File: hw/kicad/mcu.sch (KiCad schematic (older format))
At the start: 23 parts

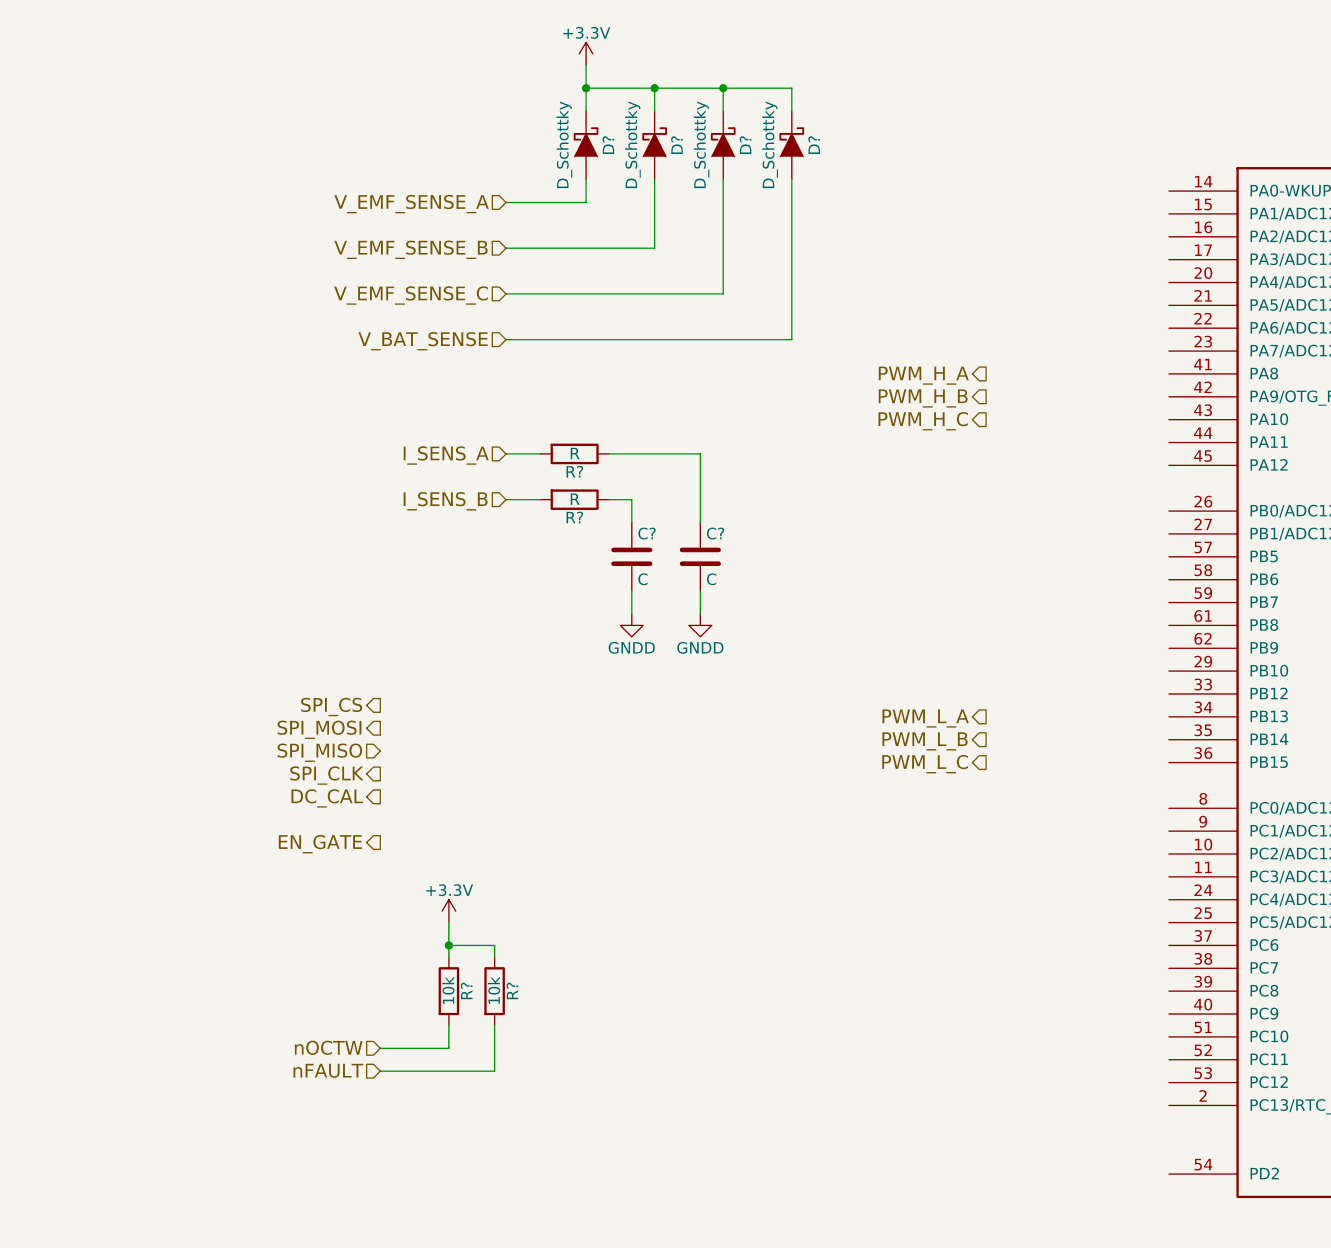
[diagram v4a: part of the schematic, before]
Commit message: Connect mcu to drv8301
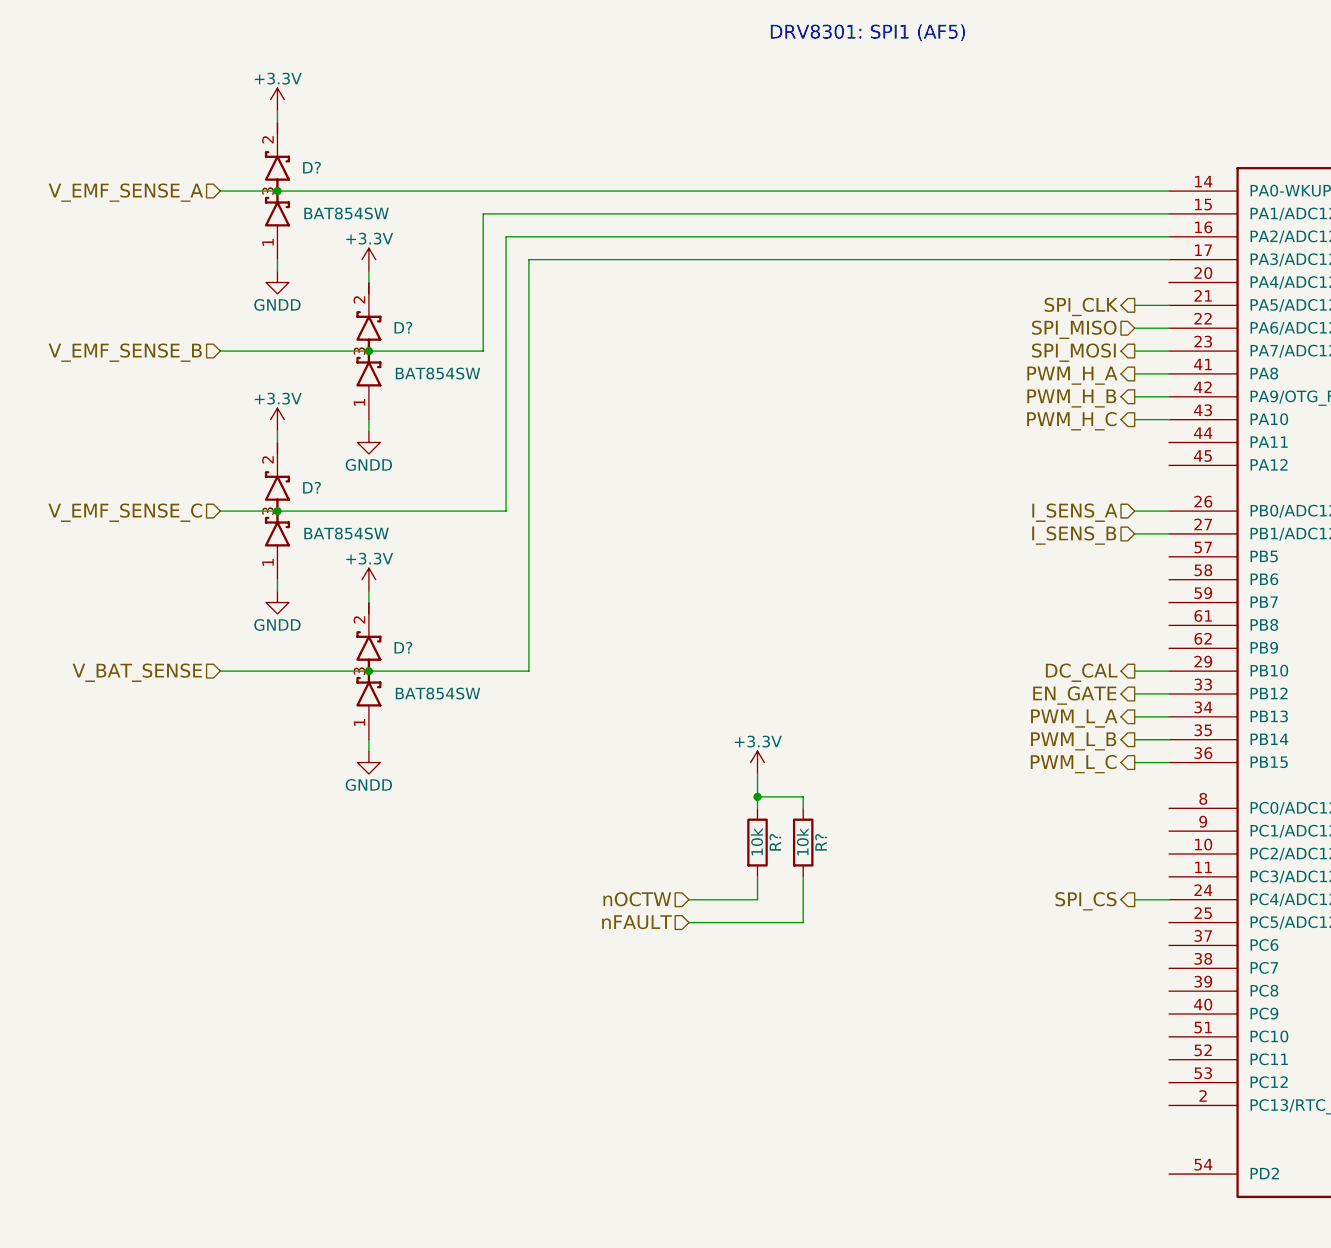
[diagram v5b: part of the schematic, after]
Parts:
- removed C? (x2): C, symbol C
- removed D? (x4): D_Schottky, symbol D_Schottky
- removed R? (x2): R, symbol R
- added D? (x4): BAT854SW, TO_SOT_Packages_SMD:SOT-323, symbol D_Schottky_x2_Serial_AKC
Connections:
- net +3V3: now also D?.2 (K), D?.2 (K), D?.2 (K), D?.2 (K)
- net DC_CAL: now also U?.29 (PB10)
- net EN_GATE: now also U?.33 (PB12)
- net GNDD: now also D?.1 (A), D?.1 (A), D?.1 (A), D?.1 (A)
- net I_SENS_A: now also U?.26 (PB0/ADC12_IN8)
- net I_SENS_B: now also U?.27 (PB1/ADC12_IN9)
- net PWM_H_A: now also U?.41 (PA8)
- net PWM_H_B: now also U?.42 (PA9/OTG_FS_VBUS)
- net PWM_H_C: now also U?.43 (PA10)
- net PWM_L_A: now also U?.34 (PB13)
- net PWM_L_B: now also U?.35 (PB14)
- net PWM_L_C: now also U?.36 (PB15)
- net SPI_CLK: now also U?.21 (PA5/ADC12_IN5/DAC_OUT2)
- net SPI_CS: now also U?.24 (PC4/ADC12_IN14)
- net SPI_MISO: now also U?.22 (PA6/ADC12_IN6)
- net SPI_MOSI: now also U?.23 (PA7/ADC12_IN7)
- net V_BAT_SENSE: now also U?.17 (PA3/ADC123_IN3), D?.3 (common)
- net V_EMF_SENSE_A: now also U?.14 (PA0-WKUP/ADC123_IN0), D?.3 (common)
- net V_EMF_SENSE_B: now also U?.15 (PA1/ADC123_IN1), D?.3 (common)
- net V_EMF_SENSE_C: now also U?.16 (PA2/ADC123_IN2), D?.3 (common)
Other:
- note added: "DRV8301: SPI1 (AF5)"
- moved on the sheet: R?

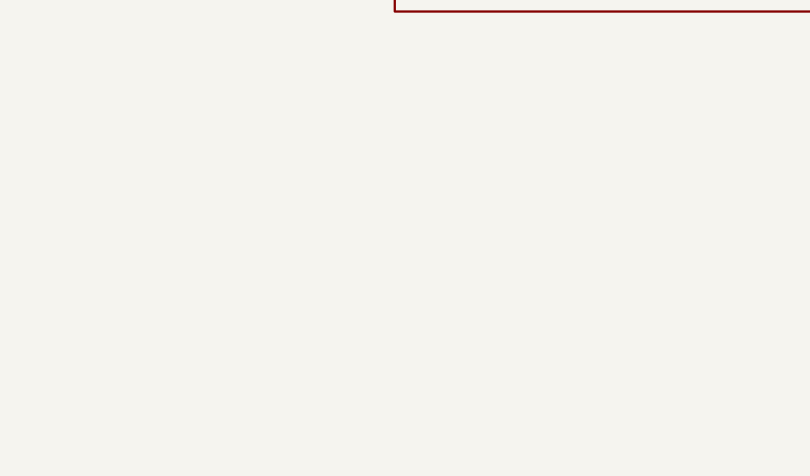
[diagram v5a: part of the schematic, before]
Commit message: Added LDO for mcu
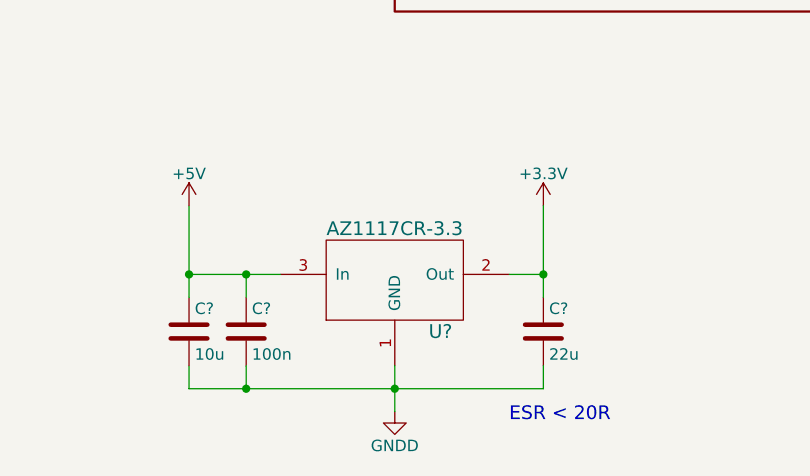
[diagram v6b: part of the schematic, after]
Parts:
- added C?: 100n, symbol C
- added C?: 22u, symbol C
- added C?: 10u, symbol C
- added U?: AZ1117CR-3.3, TO_SOT_Packages_SMD:SOT89-3_Housing, symbol AZ1117CR-3.3
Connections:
- net +3V3: now also C?.1, U?.2 (Out)
- net GNDD: now also C?.2, C?.2, C?.2, U?.1 (GND)
- new net +5V: C?.1, C?.1, U?.3 (In)
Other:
- note added: "ESR < 20R"
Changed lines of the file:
@@
 LIBS:wslp2726
 LIBS:test
+LIBS:az1117c
 LIBS:MotCtrl-cache
 EELAYER 25 0
@@
 Wire Wire Line
 	5350 3400 5500 3400
+$Comp
+L +5V #PWR?
+U 1 1 5823AFF4
+P 4900 6550
+F 0 "#PWR?" H 4900 6400 50  0001 C CNN
+F 1 "+5V" H 4900 6690 50  0000 C CNN
+F 2 "" H 4900 6550 60  0000 C CNN
+F 3 "" H 4900 6550 60  0000 C CNN
+	1    4900 6550
+	1    0    0    -1
+$EndComp
+$Comp
+L +3.3V #PWR?
+U 1 1 5823B078
+P 6450 6550
+F 0 "#PWR?" H 6450 6400 50  0001 C CNN
+F 1 "+3.3V" H 6450 6690 50  0000 C CNN
+F 2 "" H 6450 6550 60  0000 C CNN
+F 3 "" H 6450 6550 60  0000 C CNN
+	1    6450 6550
+	1    0    0    -1
+$EndComp
+$Comp
+L GNDD #PWR?
+U 1 1 5823B0BC
+P 5800 7450
+F 0 "#PWR?" H 5800 7200 50  0001 C CNN
+F 1 "GNDD" H 5800 7300 50  0000 C CNN
+F 2 "" H 5800 7450 60  0000 C CNN
+F 3 "" H 5800 7450 60  0000 C CNN
+	1    5800 7450
+	1    0    0    -1
+$EndComp
+$Comp
+L AZ1117CR-3.3 U?
+U 1 1 5823B559
+P 5800 6850
+F 0 "U?" H 6000 6600 60  0000 C CNN
+F 1 "AZ1117CR-3.3" H 5800 7050 60  0000 C CNN
+F 2 "TO_SOT_Packages_SMD:SOT89-3_Housing" H 5800 6850 60  0001 C CNN
+F 3 "" H 5800 6850 60  0001 C CNN
+	1    5800 6850
+	1    0    0    -1
+$EndComp
+$Comp
+L C C?
+U 1 1 5823B6C8
+P 5150 7100
+F 0 "C?" H 5175 7200 50  0000 L CNN
+F 1 "100n" H 5175 7000 50  0000 L CNN
+F 2 "" H 5188 6950 30  0000 C CNN
+F 3 "" H 5150 7100 60  0000 C CNN
+	1    5150 7100
+	1    0    0    -1
+$EndComp
+$Comp
+L C C?
+U 1 1 5823B818
+P 6450 7100
+F 0 "C?" H 6475 7200 50  0000 L CNN
+F 1 "22u" H 6475 7000 50  0000 L CNN
+F 2 "" H 6488 6950 30  0000 C CNN
+F 3 "" H 6450 7100 60  0000 C CNN
+	1    6450 7100
+	1    0    0    -1
+$EndComp
+Wire Wire Line
+	5150 6950 5150 6850
+Wire Wire Line
+	4900 6850 5300 6850
+Wire Wire Line
+	6300 6850 6450 6850
+Wire Wire Line
+	6450 6550 6450 6950
+Wire Wire Line
+	5800 7450 5800 7250
+Wire Wire Line
+	4900 7350 6450 7350
+Wire Wire Line
+	6450 7350 6450 7250
+Connection ~ 5800 7350
+Wire Wire Line
+	5150 7350 5150 7250
+$Comp
+L C C?
+U 1 1 5823BE21
+P 4900 7100
+F 0 "C?" H 4925 7200 50  0000 L CNN
+F 1 "10u" H 4925 7000 50  0000 L CNN
+F 2 "" H 4938 6950 30  0000 C CNN
+F 3 "" H 4900 7100 60  0000 C CNN
+	1    4900 7100
+	1    0    0    -1
+$EndComp
+Wire Wire Line
+	4900 7350 4900 7250
+Connection ~ 5150 7350
+Wire Wire Line
+	4900 6550 4900 6950
+Connection ~ 5150 6850
+Connection ~ 4900 6850
+Connection ~ 6450 6850
+Text Notes 6300 7500 0    60   ~ 0
+ESR < 20R
 $EndSCHEMATC

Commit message: work
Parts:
- added C? (x4): 4n7, symbol C
- added P?: CONN_01X06, symbol CONN_01X06
- added R? (x3): 2k2, symbol R
- added R? (x4): 10k, symbol R
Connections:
- net +3V3: now also R?.1, R?.1, R?.1, R?.1
- net +5V: now also P?.1 (P1)
- net GNDD: now also C?.2, C?.2, C?.2, C?.2, P?.6 (P6)
- new net: P?.3 (P3), R?.2, R?.2
- new net: P?.4 (P4), R?.2, R?.2
- new net: P?.5 (P5), R?.2, R?.2
- new net HALL_1: C?.1, R?.1
- new net HALL_2: C?.1, R?.1
- new net HALL_3: C?.1, R?.1
- new net MOT_TEMP: C?.1, P?.2 (P2), R?.2
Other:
- moved on the sheet: R?

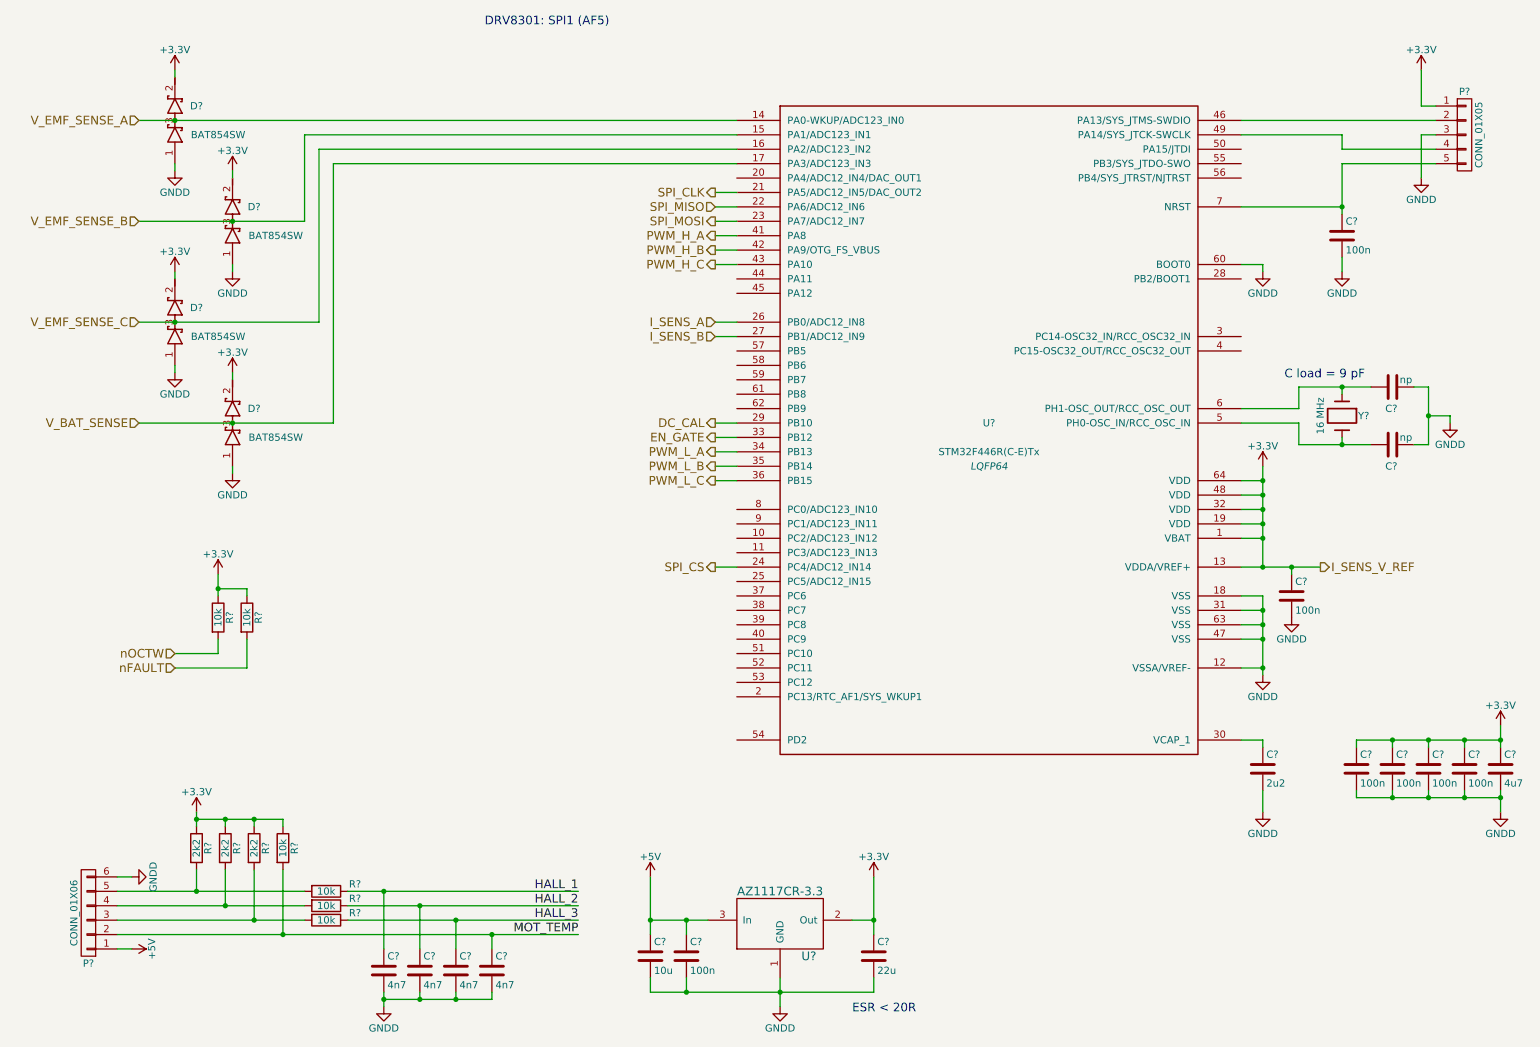
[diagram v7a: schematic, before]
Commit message: Big changes in power: new mosfets, drivers and current sensing
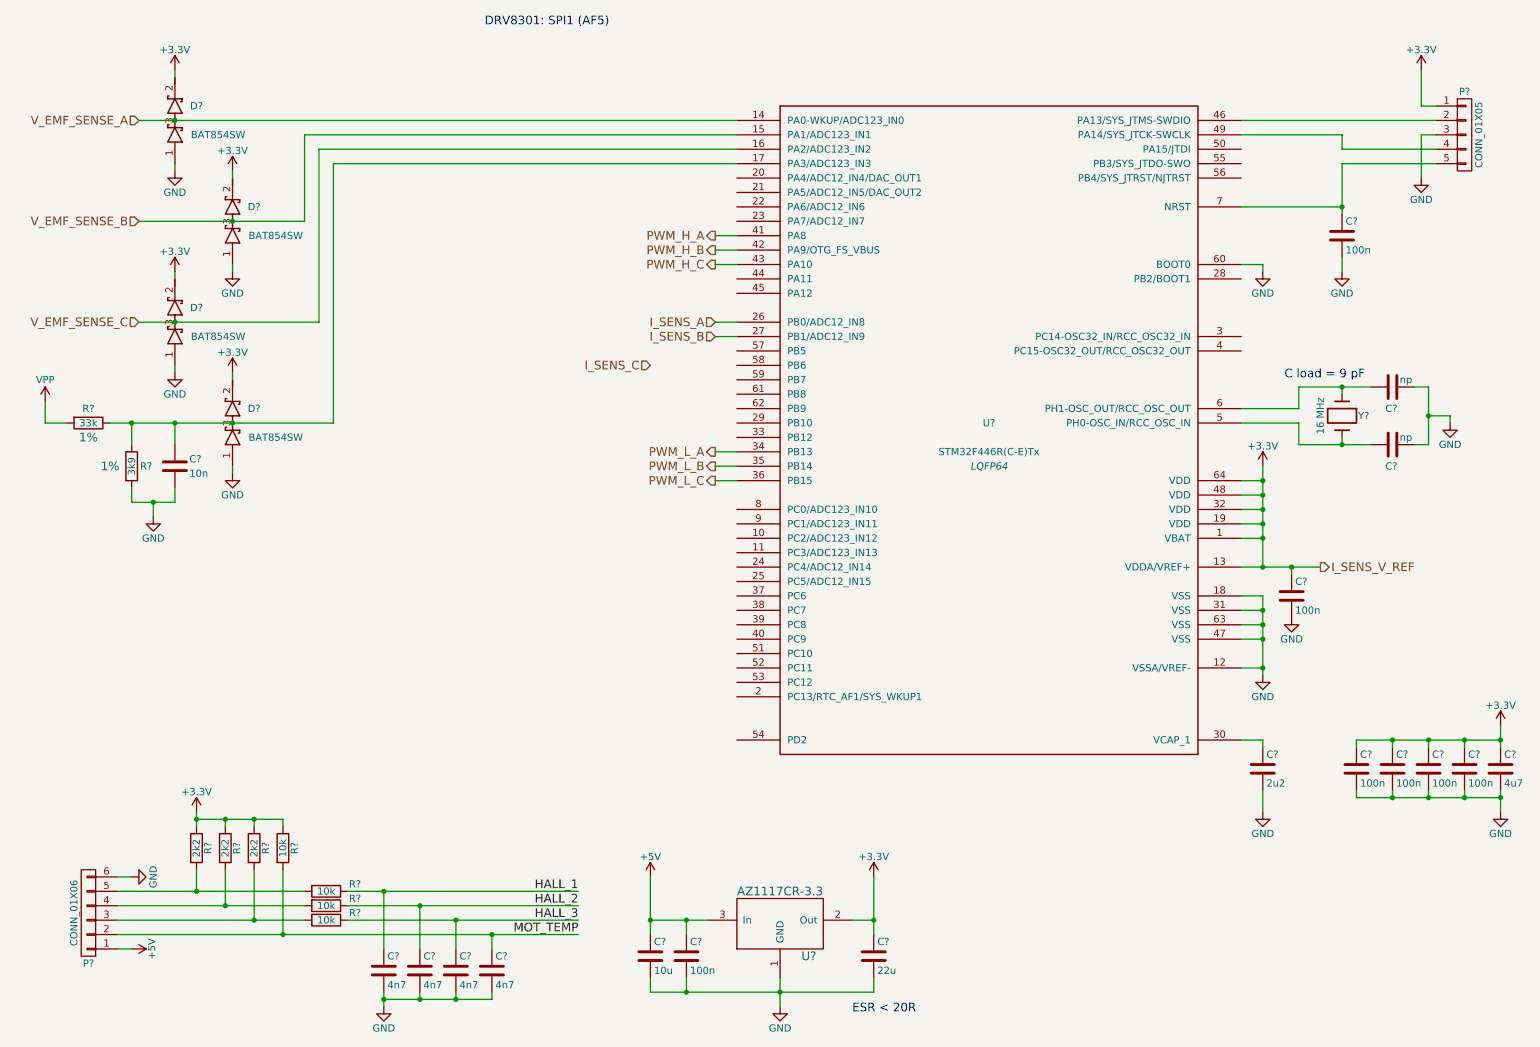
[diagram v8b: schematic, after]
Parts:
- removed R? (x2): 10k, symbol R
- added C?: 10n, symbol C
- added R?: 33k, symbol R
- added R?: 3k9, symbol R
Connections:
- net DC_CAL: no longer names the net of U?.29 (PB10)
- net EN_GATE: no longer names the net of U?.33 (PB12)
- net GNDD renamed GND
- net GND: now also C?.2, R?.2
- net SPI_CLK: no longer names the net of U?.21 (PA5/ADC12_IN5/DAC_OUT2)
- net SPI_CS: no longer names the net of U?.24 (PC4/ADC12_IN14)
- net SPI_MISO: no longer names the net of U?.22 (PA6/ADC12_IN6)
- net SPI_MOSI: no longer names the net of U?.23 (PA7/ADC12_IN7)
- net V_BAT_SENSE: no longer names the net of D?.3 (common), U?.17 (PA3/ADC123_IN3)
- net V_BAT_SENSE: now also C?.1, R?.1, R?.1
- new net VPP: R?.2
